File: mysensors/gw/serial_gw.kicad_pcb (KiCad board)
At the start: 2 copper layers, 44.5 x 19.8 mm, 69 parts, among them CON1 AVR-ISP-6, IC1 ATMEGA328P-MU, P1 USB_A, P2 ANTENNA, SW1 RESET, U1 TXB0104, U2 MCP1703A-3302, U3 CP2102, U4 RFM69W, U5 ATSHA204A, X1 16MHz

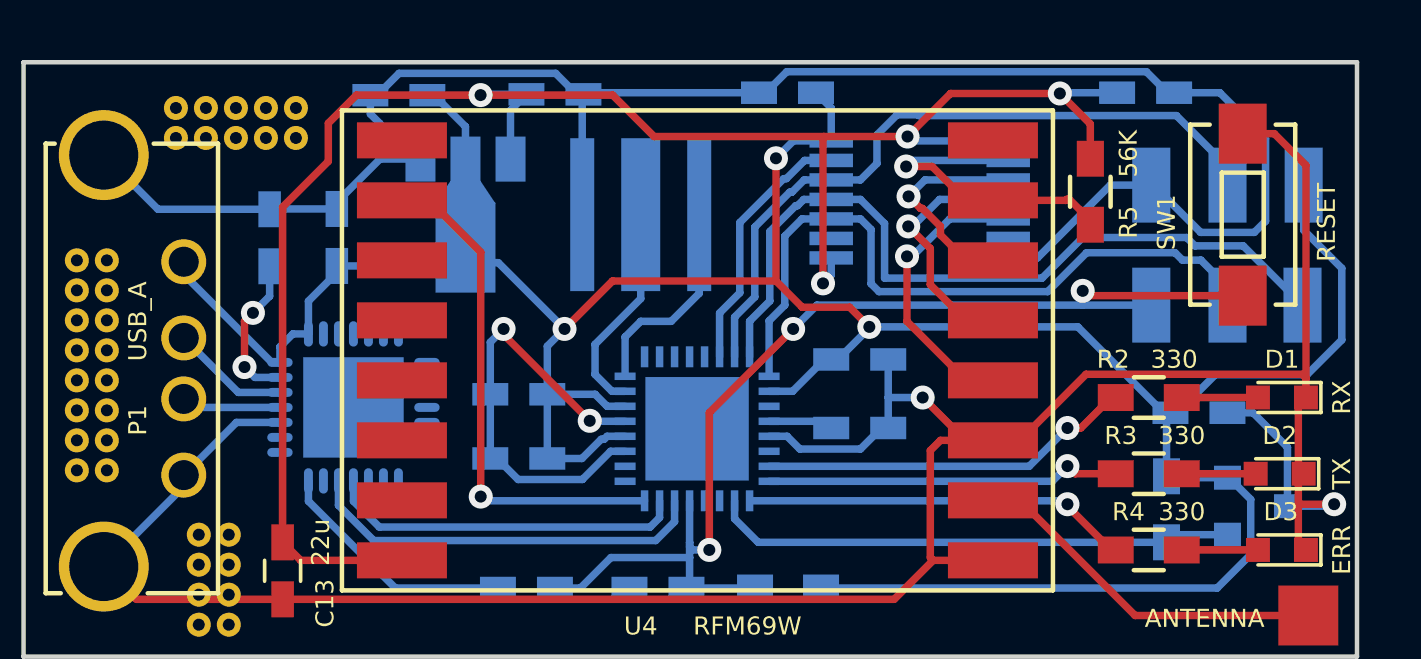
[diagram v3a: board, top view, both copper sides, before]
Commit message: [mysensors_gw] pcb routing - 3rd pass
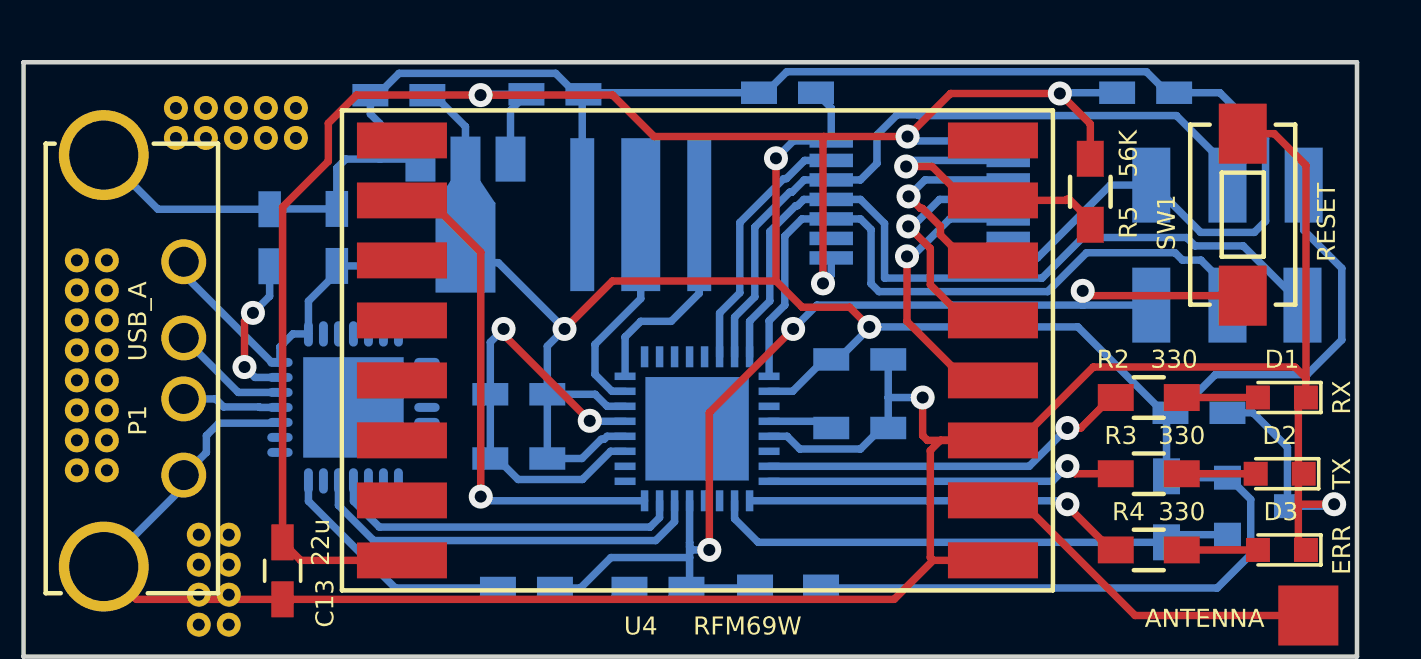
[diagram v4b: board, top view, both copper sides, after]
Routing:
- net GND: track 168.3 -> 170.2 mm
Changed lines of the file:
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@@
     (thickness 1.6)
     (drawings 11)
-    (tracks 380)
+    (tracks 388)
     (zones 0)
     (modules 69)
@@
     (last_trace_width 0.25)
     (trace_clearance 0.2)
-    (zone_clearance 0.508)
+    (zone_clearance 0.5)
     (zone_45_only no)
     (trace_min 0.2)
@@
   (gr_line (start 115.316 73.66) (end 115.316 93.472) (layer Edge.Cuts) (width 0.15))
   (gr_line (start 70.866 73.66) (end 115.316 73.66) (layer Edge.Cuts) (width 0.15))
+  (segment (start 82.74666 76.88834) (end 81.60766 76.88834) (width 0.25) (layer B.Cu) (net 1))
+  (segment (start 81.60766 76.88834) (end 81.31 77.186) (width 0.25) (layer B.Cu) (net 1))
+  (segment (start 81.31 77.186) (end 81.31 78.55) (width 0.25) (layer B.Cu) (net 1))
+  (segment (start 100.838 84.836) (end 100.838 86.106) (width 0.25) (layer F.Cu) (net 1))
+  (segment (start 100.838 86.106) (end 100.996 86.264) (width 0.25) (layer F.Cu) (net 1))
+  (segment (start 100.996 86.264) (end 103.18 86.264) (width 0.25) (layer F.Cu) (net 1))
+  (segment (start 79.4135 85.6655) (end 79.38851 85.69049) (width 0.25) (layer B.Cu) (net 1))
+  (segment (start 79.38851 85.69049) (end 77.37751 85.69049) (width 0.25) (layer B.Cu) (net 1))
+  (segment (start 76.962 86.106) (end 76.962 86.667) (width 0.25) (layer B.Cu) (net 1))
+  (segment (start 77.37751 85.69049) (end 76.962 86.106) (width 0.25) (layer B.Cu) (net 1))
+  (segment (start 76.962 86.667) (end 76.207 87.422) (width 0.25) (layer B.Cu) (net 1))
+  (segment (start 113.614 84.186) (end 113.248 83.82) (width 0.25) (layer F.Cu) (net 1))
+  (segment (start 113.248 83.82) (end 106.524 83.82) (width 0.25) (layer F.Cu) (net 1))
+  (segment (start 106.524 83.82) (end 104.08 86.264) (width 0.25) (layer F.Cu) (net 1))
+  (segment (start 104.08 86.264) (end 103.18 86.264) (width 0.25) (layer F.Cu) (net 1))
   (segment (start 89.49 78.74) (end 89.49 74.77) (width 0.25) (layer B.Cu) (net 1) (status 30))
   (segment (start 89.49 74.77) (end 89.53 74.73) (width 0.25) (layer B.Cu) (net 1) (status 30))
@@
   (via (at 114.554 88.392) (size 0.8) (drill 0.4) (layers F.Cu B.Cu) (net 1))
   (segment (start 114.488 88.458) (end 114.554 88.392) (width 0.25) (layer B.Cu) (net 1))
-  (segment (start 113.614 84.186) (end 113.488999 84.060999) (width 0.25) (layer F.Cu) (net 1))
-  (segment (start 113.488999 84.060999) (end 106.283001 84.060999) (width 0.25) (layer F.Cu) (net 1))
-  (segment (start 106.283001 84.060999) (end 104.08 86.264) (width 0.25) (layer F.Cu) (net 1) (status 20))
-  (segment (start 104.08 86.264) (end 103.18 86.264) (width 0.25) (layer F.Cu) (net 1) (status 30))
   (segment (start 109.22 74.676) (end 108.995 74.676) (width 0.25) (layer B.Cu) (net 1) (status 30))
   (segment (start 108.995 74.676) (end 108.294999 73.975999) (width 0.25) (layer B.Cu) (net 1) (status 10))
@@
   (segment (start 96.307001 73.975999) (end 95.607 74.676) (width 0.25) (layer B.Cu) (net 1) (status 20))
   (segment (start 95.607 74.676) (end 95.382 74.676) (width 0.25) (layer B.Cu) (net 1) (status 30))
-  (segment (start 100.838 84.836) (end 102.266 86.264) (width 0.25) (layer F.Cu) (net 1) (status 20))
-  (segment (start 102.266 86.264) (end 103.18 86.264) (width 0.25) (layer F.Cu) (net 1) (status 30))
   (segment (start 99.69 84.836) (end 99.69 85.852) (width 0.25) (layer B.Cu) (net 1) (status 20))
   (segment (start 99.69 83.566) (end 99.69 84.836) (width 0.25) (layer B.Cu) (net 1) (status 10))
@@
   (segment (start 79.08 78.55) (end 79.07 78.56) (width 0.25) (layer B.Cu) (net 1) (status 30))
   (segment (start 84.09686 76.88834) (end 82.74666 76.88834) (width 0.25) (layer B.Cu) (net 1) (status 10))
-  (segment (start 82.74666 76.88834) (end 81.31 78.325) (width 0.25) (layer B.Cu) (net 1) (status 20))
-  (segment (start 81.31 78.325) (end 81.31 78.55) (width 0.25) (layer B.Cu) (net 1) (status 30))
   (segment (start 103.69 80.182) (end 104.665 80.182) (width 0.25) (layer B.Cu) (net 1) (status 10))
   (segment (start 104.665 80.182) (end 107.091 77.756) (width 0.25) (layer B.Cu) (net 1))
@@
   (segment (start 113.36 84.836) (end 113.36 87.3) (width 0.25) (layer F.Cu) (net 1) (status 30))
   (segment (start 113.36 87.3) (end 113.284 87.376) (width 0.25) (layer F.Cu) (net 1) (status 30))
-  (segment (start 79.4135 85.6655) (end 77.9635 85.6655) (width 0.25) (layer B.Cu) (net 1) (status 10))
-  (segment (start 77.9635 85.6655) (end 76.207 87.422) (width 0.25) (layer B.Cu) (net 1) (status 20))
   (segment (start 88.9 82.55) (end 86.6902 80.3402) (width 0.25) (layer B.Cu) (net 2))
   (segment (start 86.6902 80.3402) (end 85.598 80.3402) (width 0.25) (layer B.Cu) (net 2) (status 20))
@@
   (segment (start 79.4135 84.6655) (end 78.0225 84.6655) (width 0.25) (layer B.Cu) (net 14) (status 10))
   (segment (start 78.0225 84.6655) (end 76.207 82.85) (width 0.25) (layer B.Cu) (net 14) (status 20))
-  (segment (start 79.4135 85.1655) (end 76.4905 85.1655) (width 0.25) (layer B.Cu) (net 15) (status 30))
-  (segment (start 76.4905 85.1655) (end 76.207 84.882) (width 0.25) (layer B.Cu) (net 15) (status 30))
+  (segment (start 77.268466 84.882) (end 76.207 84.882) (width 0.25) (layer B.Cu) (net 15))
+  (segment (start 78.720989 85.147989) (end 77.534455 85.147989) (width 0.25) (layer B.Cu) (net 15))
+  (segment (start 78.7385 85.1655) (end 78.720989 85.147989) (width 0.25) (layer B.Cu) (net 15))
+  (segment (start 79.4135 85.1655) (end 78.7385 85.1655) (width 0.25) (layer B.Cu) (net 15))
+  (segment (start 77.534455 85.147989) (end 77.268466 84.882) (width 0.25) (layer B.Cu) (net 15))
   (segment (start 104.08 88.264) (end 107.918 92.102) (width 0.25) (layer F.Cu) (net 16) (status 10))
   (segment (start 103.18 88.264) (end 104.08 88.264) (width 0.25) (layer F.Cu) (net 16) (status 30))
@@
   (segment (start 96.295577 77.539992) (end 96.903569 76.932) (width 0.25) (layer B.Cu) (net 30))
   (zone (net 1) (net_name GND) (layer B.Cu) (hatch edge 0.508)
-    (connect_pads (clearance 0.508))
+    (connect_pads (clearance 0.5))
     (min_thickness 0.254)
-    (fill yes (arc_segments 16) (thermal_gap 0.508) (thermal_bridge_width 0.508))
+    (fill yes (arc_segments 16) (thermal_gap 0.5) (thermal_bridge_width 0.5))
     (polygon
       (pts
@@
   )
   (zone (net 1) (net_name GND) (layer F.Cu) (hatch edge 0.508)
-    (connect_pads (clearance 0.508))
+    (connect_pads (clearance 0.5))
     (min_thickness 0.254)
-    (fill yes (arc_segments 16) (thermal_gap 0.508) (thermal_bridge_width 0.508))
+    (fill yes (arc_segments 16) (thermal_gap 0.5) (thermal_bridge_width 0.5))
     (polygon
       (pts

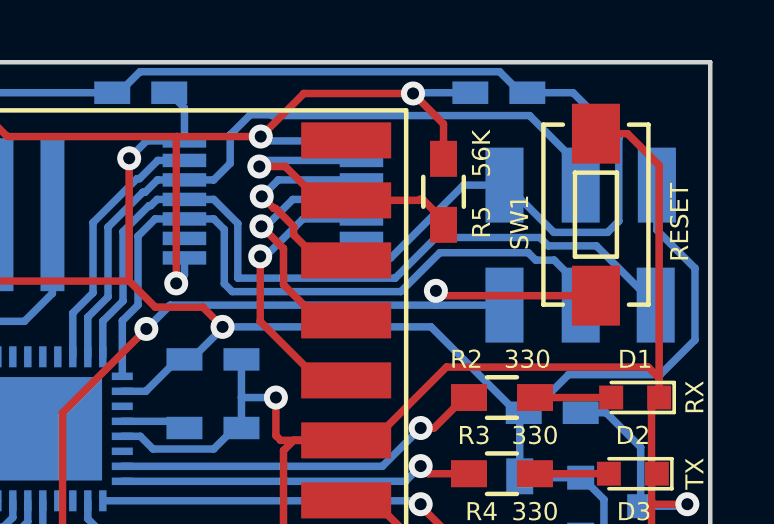
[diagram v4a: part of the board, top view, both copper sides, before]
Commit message: [mysensors_gw] pcb routing - some estetic touches
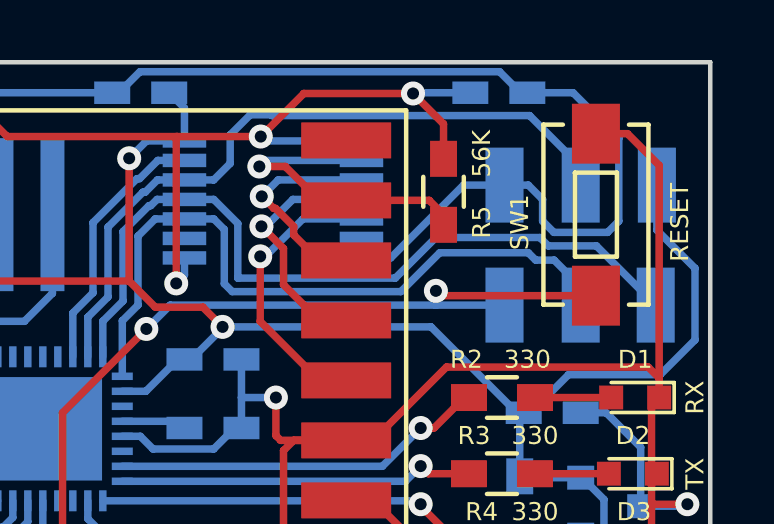
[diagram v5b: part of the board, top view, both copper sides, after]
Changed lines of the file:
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@@
   (gr_line (start 115.316 73.66) (end 115.316 93.472) (layer Edge.Cuts) (width 0.15))
   (gr_line (start 70.866 73.66) (end 115.316 73.66) (layer Edge.Cuts) (width 0.15))
+  (segment (start 108.458 77.756) (end 109.252 77.756) (width 0.25) (layer B.Cu) (net 1))
+  (segment (start 109.252 77.756) (end 109.728 78.232) (width 0.25) (layer B.Cu) (net 1))
+  (segment (start 109.728 78.232) (end 109.728 78.956002) (width 0.25) (layer B.Cu) (net 1))
+  (segment (start 112.268 76.2) (end 110.744 74.676) (width 0.25) (layer B.Cu) (net 1))
+  (segment (start 109.728 78.956002) (end 110.102999 79.331001) (width 0.25) (layer B.Cu) (net 1))
+  (segment (start 110.102999 79.331001) (end 111.893001 79.331001) (width 0.25) (layer B.Cu) (net 1))
+  (segment (start 112.268 78.956002) (end 112.268 76.2) (width 0.25) (layer B.Cu) (net 1))
+  (segment (start 111.893001 79.331001) (end 112.268 78.956002) (width 0.25) (layer B.Cu) (net 1))
+  (segment (start 110.744 74.676) (end 109.22 74.676) (width 0.25) (layer B.Cu) (net 1))
   (segment (start 82.74666 76.88834) (end 81.60766 76.88834) (width 0.25) (layer B.Cu) (net 1))
   (segment (start 81.60766 76.88834) (end 81.31 77.186) (width 0.25) (layer B.Cu) (net 1))
@@
   (segment (start 89.755566 85.628) (end 89.739632 85.612066) (width 0.25) (layer B.Cu) (net 1))
   (via (at 89.739632 85.612066) (size 0.8) (drill 0.4) (layers F.Cu B.Cu) (net 1))
-  (segment (start 108.458 77.756) (end 108.527998 77.756) (width 0.25) (layer B.Cu) (net 1) (status 30))
-  (segment (start 108.527998 77.756) (end 110.102999 79.331001) (width 0.25) (layer B.Cu) (net 1) (status 10))
-  (segment (start 110.102999 79.331001) (end 111.893001 79.331001) (width 0.25) (layer B.Cu) (net 1))
-  (segment (start 110.744 74.676) (end 109.22 74.676) (width 0.25) (layer B.Cu) (net 1) (status 20))
-  (segment (start 111.893001 79.331001) (end 112.268 78.956002) (width 0.25) (layer B.Cu) (net 1))
-  (segment (start 112.268 78.956002) (end 112.268 76.2) (width 0.25) (layer B.Cu) (net 1))
-  (segment (start 112.268 76.2) (end 110.744 74.676) (width 0.25) (layer B.Cu) (net 1))
   (segment (start 103.18 86.264) (end 101.43 86.264) (width 0.25) (layer F.Cu) (net 1) (status 10))
   (segment (start 101.43 86.264) (end 101.092 86.602) (width 0.25) (layer F.Cu) (net 1))
@@
   (segment (start 105.664 88.456) (end 105.664 88.392) (width 0.25) (layer F.Cu) (net 19))
   (segment (start 95.0685 88.278) (end 105.55 88.278) (width 0.25) (layer B.Cu) (net 19) (status 10))
+  (segment (start 103.18 78.264) (end 105.95 78.264) (width 0.25) (layer F.Cu) (net 20))
+  (segment (start 105.95 78.264) (end 106.426 78.74) (width 0.25) (layer F.Cu) (net 20))
+  (segment (start 106.426 78.74) (end 106.426 79.078) (width 0.25) (layer F.Cu) (net 20))
   (segment (start 100.489319 76.932) (end 100.286258 77.135061) (width 0.25) (layer B.Cu) (net 20))
   (via (at 100.286258 77.135061) (size 0.8) (drill 0.4) (layers F.Cu B.Cu) (net 20))
@@
   (segment (start 103.69 76.932) (end 100.489319 76.932) (width 0.25) (layer B.Cu) (net 20) (status 10))
   (segment (start 103.18 78.264) (end 102.28 78.264) (width 0.25) (layer F.Cu) (net 20) (status 30))
-  (segment (start 103.18 78.264) (end 105.612 78.264) (width 0.25) (layer F.Cu) (net 20) (status 10))
-  (segment (start 105.612 78.264) (end 105.648 78.228) (width 0.25) (layer F.Cu) (net 20))
-  (segment (start 105.648 78.228) (end 105.726 78.228) (width 0.25) (layer F.Cu) (net 20))
-  (segment (start 105.726 78.228) (end 106.426 78.928) (width 0.25) (layer F.Cu) (net 20) (status 20))
-  (segment (start 106.426 78.928) (end 106.426 79.078) (width 0.25) (layer F.Cu) (net 20) (status 30))
   (via (at 100.315316 80.130968) (size 0.8) (drill 0.4) (layers F.Cu B.Cu) (net 21))
   (segment (start 102.28 84.264) (end 100.315316 82.299316) (width 0.25) (layer F.Cu) (net 21) (status 10))
@@
       )
     )
+  )
+  (zone (net 0) (net_name "") (layer F.Cu) (hatch edge 0.508)
+    (connect_pads (clearance 0.55))
+    (min_thickness 0.254)
+    (keepout (tracks allowed) (vias allowed) (copperpour not_allowed))
+    (fill yes (arc_segments 16) (thermal_gap 0.55) (thermal_bridge_width 0.55))
+    (polygon
+      (pts
+        (xy 106.68 85.598) (xy 114.808 85.598) (xy 114.808 89.408) (xy 106.68 89.408)
+      )
+    )

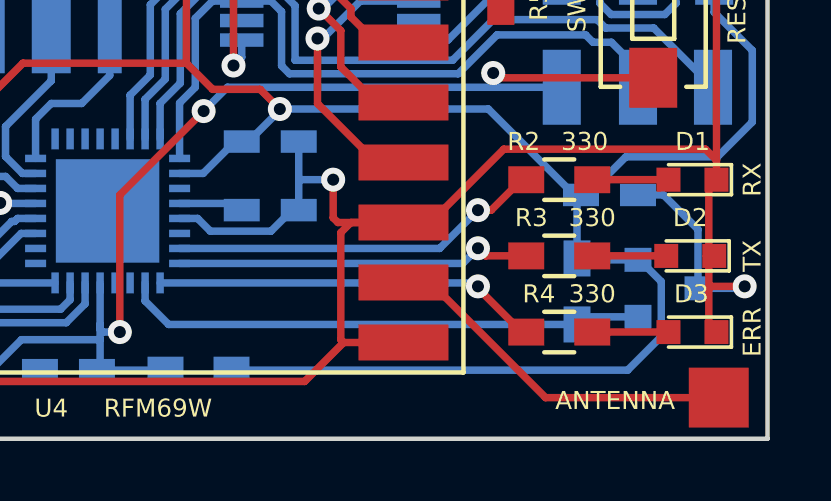
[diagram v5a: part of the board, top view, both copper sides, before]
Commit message: [mysensors_gw] pcb routing - some estetic touches
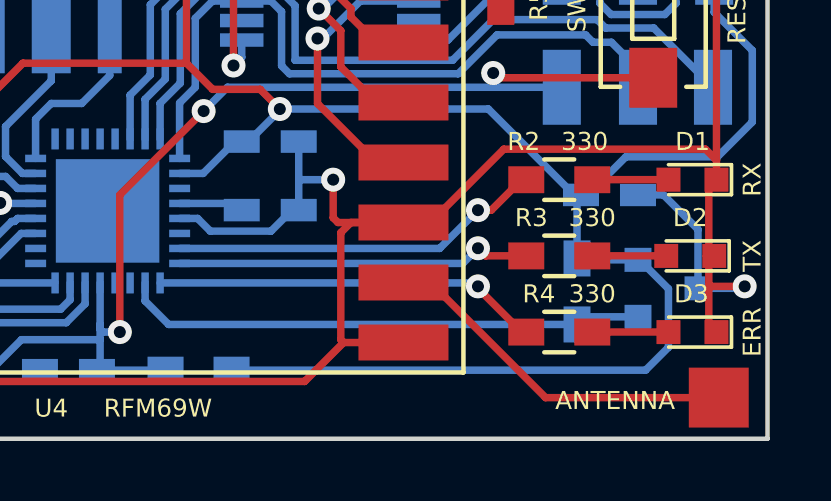
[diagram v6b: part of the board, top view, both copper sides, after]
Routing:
- net +5V: track 105.2 -> 105.8 mm
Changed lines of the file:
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@@
   (segment (start 113.36 84.836) (end 113.36 87.3) (width 0.25) (layer F.Cu) (net 1) (status 30))
   (segment (start 113.36 87.3) (end 113.284 87.376) (width 0.25) (layer F.Cu) (net 1) (status 30))
+  (segment (start 97.45 91.186) (end 111.252 91.186) (width 0.25) (layer B.Cu) (net 2))
+  (segment (start 111.252 91.186) (end 112.014 90.424) (width 0.25) (layer B.Cu) (net 2))
+  (segment (start 112.014 90.424) (end 112.014 88.474) (width 0.25) (layer B.Cu) (net 2))
+  (segment (start 112.014 88.474) (end 111.048 87.508) (width 0.25) (layer B.Cu) (net 2))
+  (segment (start 111.048 87.508) (end 110.998 87.508) (width 0.25) (layer B.Cu) (net 2))
   (segment (start 88.9 82.55) (end 86.6902 80.3402) (width 0.25) (layer B.Cu) (net 2))
   (segment (start 86.6902 80.3402) (end 85.598 80.3402) (width 0.25) (layer B.Cu) (net 2) (status 20))
@@
   (segment (start 76.2 80.727) (end 76.2 80.317) (width 0.25) (layer B.Cu) (net 2) (status 30))
   (segment (start 76.2 80.317) (end 76.207 80.31) (width 0.25) (layer B.Cu) (net 2) (status 30))
-  (segment (start 97.45 91.186) (end 110.655002 91.186) (width 0.25) (layer B.Cu) (net 2) (status 10))
-  (segment (start 110.655002 91.186) (end 111.773001 90.068001) (width 0.25) (layer B.Cu) (net 2))
-  (segment (start 111.773001 90.068001) (end 111.773001 88.233001) (width 0.25) (layer B.Cu) (net 2))
-  (segment (start 111.773001 88.233001) (end 111.048 87.508) (width 0.25) (layer B.Cu) (net 2) (status 20))
-  (segment (start 111.048 87.508) (end 110.998 87.508) (width 0.25) (layer B.Cu) (net 2) (status 30))
   (segment (start 113.538 77.756) (end 113.538 79.256) (width 0.25) (layer B.Cu) (net 2) (status 10))
   (segment (start 113.538 79.256) (end 114.808 80.526) (width 0.25) (layer B.Cu) (net 2))
